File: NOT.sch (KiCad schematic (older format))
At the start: 2 parts, among them U5 4069, U6 4069

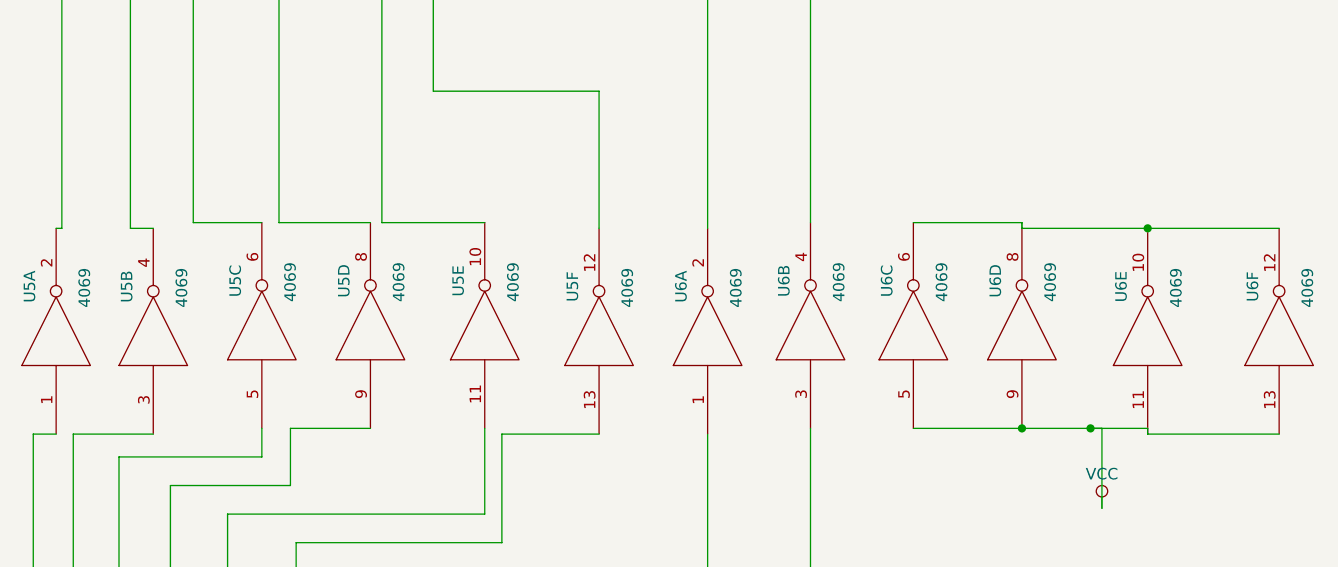
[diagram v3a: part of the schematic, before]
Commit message: fixed duplicate names
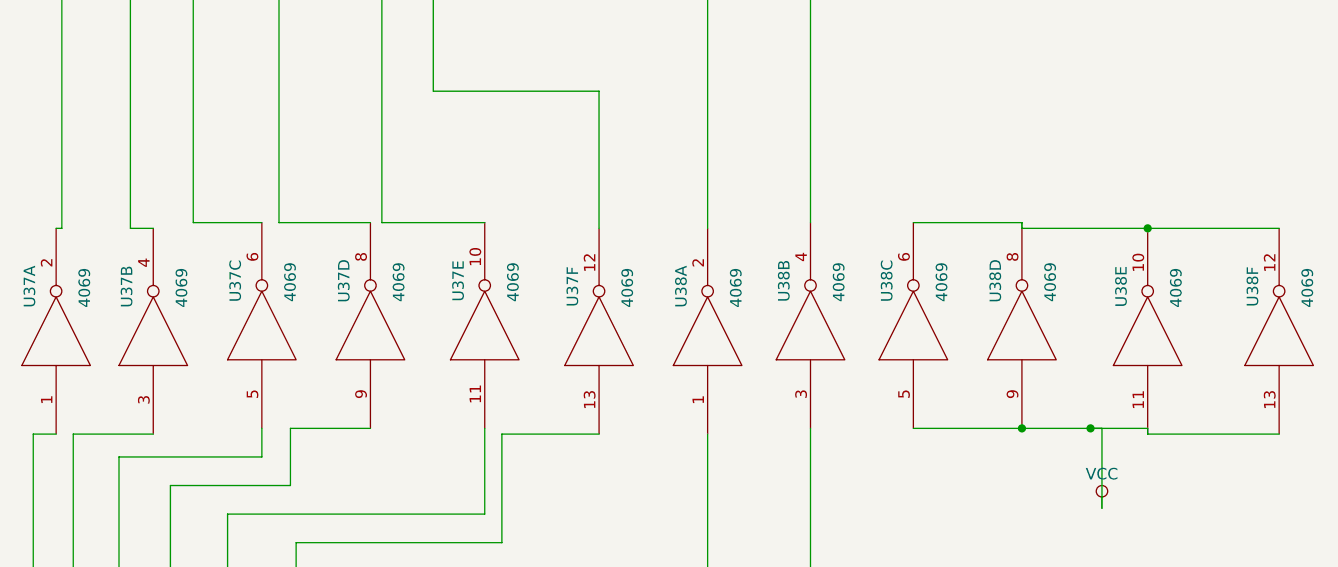
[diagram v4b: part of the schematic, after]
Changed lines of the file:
@@
 $Descr A4 11693 8268
 encoding utf-8
-Sheet 5 21
+Sheet 21 21
 Title ""
 Date ""
@@
 U 1 1 5AE664B9
 P 1025 4250
-F 0 "U5" H 1220 4365 50  0000 C CNN
+AR Path="/5AE62FB7/5AE6649D/5AE664B9" Ref="U5"  Part="1"
+AR Path="/5AE62FB7/5B1BA146/5AE664B9" Ref="U37"  Part="1"
+F 0 "U37" H 1220 4365 50  0000 C CNN
 F 1 "4069" H 1215 4125 50  0000 C CNN
 F 2 "" H 1025 4250 60  0001 C CNN
@@
 U 2 1 5AE6656E
 P 1450 4250
-F 0 "U5" H 1645 4365 50  0000 C CNN
+AR Path="/5AE62FB7/5AE6649D/5AE6656E" Ref="U5"  Part="2"
+AR Path="/5AE62FB7/5B1BA146/5AE6656E" Ref="U37"  Part="2"
+F 0 "U37" H 1645 4365 50  0000 C CNN
 F 1 "4069" H 1640 4125 50  0000 C CNN
 F 2 "" H 1450 4250 60  0001 C CNN
@@
 U 3 1 5AE66605
 P 1925 4225
-F 0 "U5" H 2120 4340 50  0000 C CNN
+AR Path="/5AE62FB7/5AE6649D/5AE66605" Ref="U5"  Part="3"
+AR Path="/5AE62FB7/5B1BA146/5AE66605" Ref="U37"  Part="3"
+F 0 "U37" H 2120 4340 50  0000 C CNN
 F 1 "4069" H 2115 4100 50  0000 C CNN
 F 2 "" H 1925 4225 60  0001 C CNN
@@
 U 4 1 5AE6667C
 P 2400 4225
-F 0 "U5" H 2595 4340 50  0000 C CNN
+AR Path="/5AE62FB7/5AE6649D/5AE6667C" Ref="U5"  Part="4"
+AR Path="/5AE62FB7/5B1BA146/5AE6667C" Ref="U37"  Part="4"
+F 0 "U37" H 2595 4340 50  0000 C CNN
 F 1 "4069" H 2590 4100 50  0000 C CNN
 F 2 "" H 2400 4225 60  0001 C CNN
@@
 U 5 1 5AE66711
 P 2900 4225
-F 0 "U5" H 3095 4340 50  0000 C CNN
+AR Path="/5AE62FB7/5AE6649D/5AE66711" Ref="U5"  Part="5"
+AR Path="/5AE62FB7/5B1BA146/5AE66711" Ref="U37"  Part="5"
+F 0 "U37" H 3095 4340 50  0000 C CNN
 F 1 "4069" H 3090 4100 50  0000 C CNN
 F 2 "" H 2900 4225 60  0001 C CNN
@@
 U 6 1 5AE667CA
 P 3400 4250
-F 0 "U5" H 3595 4365 50  0000 C CNN
+AR Path="/5AE62FB7/5AE6649D/5AE667CA" Ref="U5"  Part="6"
+AR Path="/5AE62FB7/5B1BA146/5AE667CA" Ref="U37"  Part="6"
+F 0 "U37" H 3595 4365 50  0000 C CNN
 F 1 "4069" H 3590 4125 50  0000 C CNN
 F 2 "" H 3400 4250 60  0001 C CNN
@@
 U 1 1 5AE66867
 P 3875 4250
-F 0 "U6" H 4070 4365 50  0000 C CNN
+AR Path="/5AE62FB7/5AE6649D/5AE66867" Ref="U6"  Part="1"
+AR Path="/5AE62FB7/5B1BA146/5AE66867" Ref="U38"  Part="1"
+F 0 "U38" H 4070 4365 50  0000 C CNN
 F 1 "4069" H 4065 4125 50  0000 C CNN
 F 2 "" H 3875 4250 60  0001 C CNN
@@
 U 2 1 5AE668EC
 P 4325 4225
-F 0 "U6" H 4520 4340 50  0000 C CNN
+AR Path="/5AE62FB7/5AE6649D/5AE668EC" Ref="U6"  Part="2"
+AR Path="/5AE62FB7/5B1BA146/5AE668EC" Ref="U38"  Part="2"
+F 0 "U38" H 4520 4340 50  0000 C CNN
 F 1 "4069" H 4515 4100 50  0000 C CNN
 F 2 "" H 4325 4225 60  0001 C CNN
@@
 U 3 1 5AE66989
 P 4775 4225
-F 0 "U6" H 4970 4340 50  0000 C CNN
+AR Path="/5AE62FB7/5AE6649D/5AE66989" Ref="U6"  Part="3"
+AR Path="/5AE62FB7/5B1BA146/5AE66989" Ref="U38"  Part="3"
+F 0 "U38" H 4970 4340 50  0000 C CNN
 F 1 "4069" H 4965 4100 50  0000 C CNN
 F 2 "" H 4775 4225 60  0001 C CNN
@@
 U 4 1 5AE66A24
 P 5250 4225
-F 0 "U6" H 5445 4340 50  0000 C CNN
+AR Path="/5AE62FB7/5AE6649D/5AE66A24" Ref="U6"  Part="4"
+AR Path="/5AE62FB7/5B1BA146/5AE66A24" Ref="U38"  Part="4"
+F 0 "U38" H 5445 4340 50  0000 C CNN
 F 1 "4069" H 5440 4100 50  0000 C CNN
 F 2 "" H 5250 4225 60  0001 C CNN
@@
 U 5 1 5AE66A93
 P 5800 4250
-F 0 "U6" H 5995 4365 50  0000 C CNN
+AR Path="/5AE62FB7/5AE6649D/5AE66A93" Ref="U6"  Part="5"
+AR Path="/5AE62FB7/5B1BA146/5AE66A93" Ref="U38"  Part="5"
+F 0 "U38" H 5995 4365 50  0000 C CNN
 F 1 "4069" H 5990 4125 50  0000 C CNN
 F 2 "" H 5800 4250 60  0001 C CNN
@@
 U 6 1 5AE66B26
 P 6375 4250
-F 0 "U6" H 6570 4365 50  0000 C CNN
+AR Path="/5AE62FB7/5AE6649D/5AE66B26" Ref="U6"  Part="6"
+AR Path="/5AE62FB7/5B1BA146/5AE66B26" Ref="U38"  Part="6"
+F 0 "U38" H 6570 4365 50  0000 C CNN
 F 1 "4069" H 6565 4125 50  0000 C CNN
 F 2 "" H 6375 4250 60  0001 C CNN
@@
 	5800 4700 6375 4700
 $Comp
-L VCC #PWR5
+L VCC #PWR05
 U 1 1 5AE66D66
 P 5600 5025
-F 0 "#PWR5" H 5600 4875 50  0001 C CNN
+AR Path="/5AE62FB7/5AE6649D/5AE66D66" Ref="#PWR05"  Part="1"
+AR Path="/5AE62FB7/5B1BA146/5AE66D66" Ref="#PWR037"  Part="1"
+F 0 "#PWR037" H 5600 4875 50  0001 C CNN
 F 1 "VCC" H 5600 5175 50  0000 C CNN
 F 2 "" H 5600 5025 50  0000 C CNN

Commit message: NC-symbols
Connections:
- now unconnected: U6.10, U6.12, U6.6, U6.8
- no-connect marks 0 -> 4
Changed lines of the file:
@@
 	4325 1625 4325 3775
 Wire Wire Line
-	4775 3775 5250 3775
-Wire Wire Line
-	5250 3800 6375 3800
-Wire Wire Line
 	5250 3775 5250 3800
-Connection ~ 5800 3800
+NoConn ~ 4775 3775
+NoConn ~ 5250 3800
+NoConn ~ 5800 3800
+NoConn ~ 6375 3800
 $EndSCHEMATC

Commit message: spice libs from the internet, opened with new kicad 5.0.0, added spice models to components
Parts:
- U5, U6: symbol 4069 -> myCpu-rescue:4069
- U6: symbol 4069 -> myCpu-rescue:4069; Spice_Lib_File (none) -> cd4000.lib; Spice_Model (none) -> CD4069UB; Spice_Netlist_Enabled (none) -> Y; Spice_Primitive (none) -> X
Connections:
- net VCC: no longer U6.11, U6.13, U6.5, U6.9
- new net: U6.11, U6.13, U6.5, U6.9
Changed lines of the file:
@@
-EESchema Schematic File Version 2
-LIBS:spice
-LIBS:pspice
+EESchema Schematic File Version 4
 LIBS:myCpu-cache
-EELAYER 25 0
+EELAYER 26 0
 EELAYER END
 $Descr A4 11693 8268
 encoding utf-8
-Sheet 21 21
+Sheet 5 21
 Title ""
 Date ""
@@
 Z7
 $Comp
-L 4069 U5
+L myCpu-rescue:4069 U5
 U 1 1 5AE664B9
 P 1025 4250
 AR Path="/5AE62FB7/5AE6649D/5AE664B9" Ref="U5"  Part="1"
 AR Path="/5AE62FB7/5B1BA146/5AE664B9" Ref="U37"  Part="1"
-F 0 "U37" H 1220 4365 50  0000 C CNN
+AR Path="/5AE664B9" Ref="U37"  Part="1"
+F 0 "U5" H 1220 4365 50  0000 C CNN
 F 1 "4069" H 1215 4125 50  0000 C CNN
 F 2 "" H 1025 4250 60  0001 C CNN
@@
 $EndComp
 $Comp
-L 4069 U5
+L myCpu-rescue:4069 U5
 U 2 1 5AE6656E
 P 1450 4250
 AR Path="/5AE62FB7/5AE6649D/5AE6656E" Ref="U5"  Part="2"
 AR Path="/5AE62FB7/5B1BA146/5AE6656E" Ref="U37"  Part="2"
-F 0 "U37" H 1645 4365 50  0000 C CNN
+AR Path="/5AE6656E" Ref="U37"  Part="2"
+F 0 "U5" H 1645 4365 50  0000 C CNN
 F 1 "4069" H 1640 4125 50  0000 C CNN
 F 2 "" H 1450 4250 60  0001 C CNN
@@
 $EndComp
 $Comp
-L 4069 U5
+L myCpu-rescue:4069 U5
 U 3 1 5AE66605
 P 1925 4225
 AR Path="/5AE62FB7/5AE6649D/5AE66605" Ref="U5"  Part="3"
 AR Path="/5AE62FB7/5B1BA146/5AE66605" Ref="U37"  Part="3"
-F 0 "U37" H 2120 4340 50  0000 C CNN
+AR Path="/5AE66605" Ref="U37"  Part="3"
+F 0 "U5" H 2120 4340 50  0000 C CNN
 F 1 "4069" H 2115 4100 50  0000 C CNN
 F 2 "" H 1925 4225 60  0001 C CNN
@@
 $EndComp
 $Comp
-L 4069 U5
+L myCpu-rescue:4069 U5
 U 4 1 5AE6667C
 P 2400 4225
 AR Path="/5AE62FB7/5AE6649D/5AE6667C" Ref="U5"  Part="4"
 AR Path="/5AE62FB7/5B1BA146/5AE6667C" Ref="U37"  Part="4"
-F 0 "U37" H 2595 4340 50  0000 C CNN
+AR Path="/5AE6667C" Ref="U37"  Part="4"
+F 0 "U5" H 2595 4340 50  0000 C CNN
 F 1 "4069" H 2590 4100 50  0000 C CNN
 F 2 "" H 2400 4225 60  0001 C CNN
@@
 $EndComp
 $Comp
-L 4069 U5
+L myCpu-rescue:4069 U5
 U 5 1 5AE66711
 P 2900 4225
 AR Path="/5AE62FB7/5AE6649D/5AE66711" Ref="U5"  Part="5"
 AR Path="/5AE62FB7/5B1BA146/5AE66711" Ref="U37"  Part="5"
-F 0 "U37" H 3095 4340 50  0000 C CNN
+AR Path="/5AE66711" Ref="U37"  Part="5"
+F 0 "U5" H 3095 4340 50  0000 C CNN
 F 1 "4069" H 3090 4100 50  0000 C CNN
 F 2 "" H 2900 4225 60  0001 C CNN
@@
 $EndComp
 $Comp
-L 4069 U5
+L myCpu-rescue:4069 U5
 U 6 1 5AE667CA
 P 3400 4250
 AR Path="/5AE62FB7/5AE6649D/5AE667CA" Ref="U5"  Part="6"
 AR Path="/5AE62FB7/5B1BA146/5AE667CA" Ref="U37"  Part="6"
-F 0 "U37" H 3595 4365 50  0000 C CNN
+AR Path="/5AE667CA" Ref="U37"  Part="6"
+F 0 "U5" H 3595 4365 50  0000 C CNN
 F 1 "4069" H 3590 4125 50  0000 C CNN
 F 2 "" H 3400 4250 60  0001 C CNN
@@
 $EndComp
 $Comp
-L 4069 U6
+L myCpu-rescue:4069 U6
 U 1 1 5AE66867
 P 3875 4250
 AR Path="/5AE62FB7/5AE6649D/5AE66867" Ref="U6"  Part="1"
 AR Path="/5AE62FB7/5B1BA146/5AE66867" Ref="U38"  Part="1"
-F 0 "U38" H 4070 4365 50  0000 C CNN
+AR Path="/5AE66867" Ref="U38"  Part="1"
+F 0 "U6" H 4070 4365 50  0000 C CNN
 F 1 "4069" H 4065 4125 50  0000 C CNN
 F 2 "" H 3875 4250 60  0001 C CNN
@@
 $EndComp
 $Comp
-L 4069 U6
+L myCpu-rescue:4069 U6
 U 2 1 5AE668EC
 P 4325 4225
 AR Path="/5AE62FB7/5AE6649D/5AE668EC" Ref="U6"  Part="2"
 AR Path="/5AE62FB7/5B1BA146/5AE668EC" Ref="U38"  Part="2"
-F 0 "U38" H 4520 4340 50  0000 C CNN
+AR Path="/5AE668EC" Ref="U38"  Part="2"
+F 0 "U6" H 4520 4340 50  0000 C CNN
 F 1 "4069" H 4515 4100 50  0000 C CNN
 F 2 "" H 4325 4225 60  0001 C CNN
@@
 $EndComp
 $Comp
-L 4069 U6
+L myCpu-rescue:4069 U6
 U 3 1 5AE66989
 P 4775 4225
 AR Path="/5AE62FB7/5AE6649D/5AE66989" Ref="U6"  Part="3"
 AR Path="/5AE62FB7/5B1BA146/5AE66989" Ref="U38"  Part="3"
-F 0 "U38" H 4970 4340 50  0000 C CNN
+AR Path="/5AE66989" Ref="U38"  Part="3"
+F 0 "U6" H 4970 4340 50  0000 C CNN
 F 1 "4069" H 4965 4100 50  0000 C CNN
 F 2 "" H 4775 4225 60  0001 C CNN
@@
 $EndComp
 $Comp
-L 4069 U6
+L myCpu-rescue:4069 U6
 U 4 1 5AE66A24
 P 5250 4225
 AR Path="/5AE62FB7/5AE6649D/5AE66A24" Ref="U6"  Part="4"
 AR Path="/5AE62FB7/5B1BA146/5AE66A24" Ref="U38"  Part="4"
-F 0 "U38" H 5445 4340 50  0000 C CNN
+AR Path="/5AE66A24" Ref="U38"  Part="4"
+F 0 "U6" H 5445 4340 50  0000 C CNN
 F 1 "4069" H 5440 4100 50  0000 C CNN
 F 2 "" H 5250 4225 60  0001 C CNN
@@
 $EndComp
 $Comp
-L 4069 U6
+L myCpu-rescue:4069 U6
 U 5 1 5AE66A93
 P 5800 4250
 AR Path="/5AE62FB7/5AE6649D/5AE66A93" Ref="U6"  Part="5"
 AR Path="/5AE62FB7/5B1BA146/5AE66A93" Ref="U38"  Part="5"
-F 0 "U38" H 5995 4365 50  0000 C CNN
+AR Path="/5AE66A93" Ref="U38"  Part="5"
+F 0 "U6" H 5995 4365 50  0000 C CNN
 F 1 "4069" H 5990 4125 50  0000 C CNN
 F 2 "" H 5800 4250 60  0001 C CNN
@@
 $EndComp
 $Comp
-L 4069 U6
+L myCpu-rescue:4069 U6
 U 6 1 5AE66B26
 P 6375 4250
 AR Path="/5AE62FB7/5AE6649D/5AE66B26" Ref="U6"  Part="6"
 AR Path="/5AE62FB7/5B1BA146/5AE66B26" Ref="U38"  Part="6"
-F 0 "U38" H 6570 4365 50  0000 C CNN
+AR Path="/5AE66B26" Ref="U38"  Part="6"
+F 0 "U6" H 6570 4365 50  0000 C CNN
 F 1 "4069" H 6565 4125 50  0000 C CNN
 F 2 "" H 6375 4250 60  0001 C CNN
 F 3 "" H 6375 4250 60  0001 C CNN
+F 4 "X" H 6375 4250 50  0001 C CNN "Spice_Primitive"
+F 5 "CD4069UB" H 6375 4250 50  0001 C CNN "Spice_Model"
+F 6 "Y" H 6375 4250 50  0001 C CNN "Spice_Netlist_Enabled"
+F 7 "cd4000.lib" H 6375 4250 50  0001 C CNN "Spice_Lib_File"
 	6    6375 4250
 	0    -1   -1   0
@@
 	2550 5600 2550 6275
 Wire Wire Line
-	4775 4675 5800 4675
+	4775 4675 5250 4675
 Wire Wire Line
 	5800 4675 5800 4700
@@
 	5800 4700 6375 4700
 $Comp
-L VCC #PWR05
+L myCpu-rescue:VCC #PWR05
 U 1 1 5AE66D66
 P 5600 5025
 AR Path="/5AE62FB7/5AE6649D/5AE66D66" Ref="#PWR05"  Part="1"
 AR Path="/5AE62FB7/5B1BA146/5AE66D66" Ref="#PWR037"  Part="1"
-F 0 "#PWR037" H 5600 4875 50  0001 C CNN
+F 0 "#PWR05" H 5600 4875 50  0001 C CNN
 F 1 "VCC" H 5600 5175 50  0000 C CNN
 F 2 "" H 5600 5025 50  0000 C CNN
@@
 Wire Wire Line
 	5600 5025 5600 4675
-Wire Wire Line
-	5600 4675 5550 4675
-Connection ~ 5550 4675
 Connection ~ 5250 4675
 Wire Wire Line
@@
 NoConn ~ 5800 3800
 NoConn ~ 6375 3800
+Wire Wire Line
+	5250 4675 5800 4675
 $EndSCHEMATC

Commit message: lots of work done
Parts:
- renumbered U5 to U6, U6 to U7
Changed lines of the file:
@@
 $Descr A4 11693 8268
 encoding utf-8
-Sheet 5 21
+Sheet 5 81
 Title ""
 Date ""
@@
 Z7
 $Comp
-L myCpu-rescue:4069 U5
+L myCpu-rescue:4069 U6
 U 1 1 5AE664B9
 P 1025 4250
-AR Path="/5AE62FB7/5AE6649D/5AE664B9" Ref="U5"  Part="1"
-AR Path="/5AE62FB7/5B1BA146/5AE664B9" Ref="U37"  Part="1"
-AR Path="/5AE664B9" Ref="U37"  Part="1"
-F 0 "U5" H 1220 4365 50  0000 C CNN
+AR Path="/5AE62FB7/5AE6649D/5AE664B9" Ref="U6"  Part="1"
+AR Path="/5AE62FB7/5B1BA146/5AE664B9" Ref="U36"  Part="1"
+F 0 "U36" H 1220 4365 50  0000 C CNN
 F 1 "4069" H 1215 4125 50  0000 C CNN
 F 2 "" H 1025 4250 60  0001 C CNN
@@
 $EndComp
 $Comp
-L myCpu-rescue:4069 U5
+L myCpu-rescue:4069 U6
 U 2 1 5AE6656E
 P 1450 4250
-AR Path="/5AE62FB7/5AE6649D/5AE6656E" Ref="U5"  Part="2"
-AR Path="/5AE62FB7/5B1BA146/5AE6656E" Ref="U37"  Part="2"
-AR Path="/5AE6656E" Ref="U37"  Part="2"
-F 0 "U5" H 1645 4365 50  0000 C CNN
+AR Path="/5AE62FB7/5AE6649D/5AE6656E" Ref="U6"  Part="2"
+AR Path="/5AE62FB7/5B1BA146/5AE6656E" Ref="U36"  Part="2"
+F 0 "U36" H 1645 4365 50  0000 C CNN
 F 1 "4069" H 1640 4125 50  0000 C CNN
 F 2 "" H 1450 4250 60  0001 C CNN
@@
 $EndComp
 $Comp
-L myCpu-rescue:4069 U5
+L myCpu-rescue:4069 U6
 U 3 1 5AE66605
 P 1925 4225
-AR Path="/5AE62FB7/5AE6649D/5AE66605" Ref="U5"  Part="3"
-AR Path="/5AE62FB7/5B1BA146/5AE66605" Ref="U37"  Part="3"
-AR Path="/5AE66605" Ref="U37"  Part="3"
-F 0 "U5" H 2120 4340 50  0000 C CNN
+AR Path="/5AE62FB7/5AE6649D/5AE66605" Ref="U6"  Part="3"
+AR Path="/5AE62FB7/5B1BA146/5AE66605" Ref="U36"  Part="3"
+F 0 "U36" H 2120 4340 50  0000 C CNN
 F 1 "4069" H 2115 4100 50  0000 C CNN
 F 2 "" H 1925 4225 60  0001 C CNN
@@
 $EndComp
 $Comp
-L myCpu-rescue:4069 U5
+L myCpu-rescue:4069 U6
 U 4 1 5AE6667C
 P 2400 4225
-AR Path="/5AE62FB7/5AE6649D/5AE6667C" Ref="U5"  Part="4"
-AR Path="/5AE62FB7/5B1BA146/5AE6667C" Ref="U37"  Part="4"
-AR Path="/5AE6667C" Ref="U37"  Part="4"
-F 0 "U5" H 2595 4340 50  0000 C CNN
+AR Path="/5AE62FB7/5AE6649D/5AE6667C" Ref="U6"  Part="4"
+AR Path="/5AE62FB7/5B1BA146/5AE6667C" Ref="U36"  Part="4"
+F 0 "U36" H 2595 4340 50  0000 C CNN
 F 1 "4069" H 2590 4100 50  0000 C CNN
 F 2 "" H 2400 4225 60  0001 C CNN
@@
 $EndComp
 $Comp
-L myCpu-rescue:4069 U5
+L myCpu-rescue:4069 U6
 U 5 1 5AE66711
 P 2900 4225
-AR Path="/5AE62FB7/5AE6649D/5AE66711" Ref="U5"  Part="5"
-AR Path="/5AE62FB7/5B1BA146/5AE66711" Ref="U37"  Part="5"
-AR Path="/5AE66711" Ref="U37"  Part="5"
-F 0 "U5" H 3095 4340 50  0000 C CNN
+AR Path="/5AE62FB7/5AE6649D/5AE66711" Ref="U6"  Part="5"
+AR Path="/5AE62FB7/5B1BA146/5AE66711" Ref="U36"  Part="5"
+F 0 "U36" H 3095 4340 50  0000 C CNN
 F 1 "4069" H 3090 4100 50  0000 C CNN
 F 2 "" H 2900 4225 60  0001 C CNN
@@
 $EndComp
 $Comp
-L myCpu-rescue:4069 U5
+L myCpu-rescue:4069 U6
 U 6 1 5AE667CA
 P 3400 4250
-AR Path="/5AE62FB7/5AE6649D/5AE667CA" Ref="U5"  Part="6"
-AR Path="/5AE62FB7/5B1BA146/5AE667CA" Ref="U37"  Part="6"
-AR Path="/5AE667CA" Ref="U37"  Part="6"
-F 0 "U5" H 3595 4365 50  0000 C CNN
+AR Path="/5AE62FB7/5AE6649D/5AE667CA" Ref="U6"  Part="6"
+AR Path="/5AE62FB7/5B1BA146/5AE667CA" Ref="U36"  Part="6"
+F 0 "U36" H 3595 4365 50  0000 C CNN
 F 1 "4069" H 3590 4125 50  0000 C CNN
 F 2 "" H 3400 4250 60  0001 C CNN
@@
 $EndComp
 $Comp
-L myCpu-rescue:4069 U6
+L myCpu-rescue:4069 U7
 U 1 1 5AE66867
 P 3875 4250
-AR Path="/5AE62FB7/5AE6649D/5AE66867" Ref="U6"  Part="1"
-AR Path="/5AE62FB7/5B1BA146/5AE66867" Ref="U38"  Part="1"
-AR Path="/5AE66867" Ref="U38"  Part="1"
-F 0 "U6" H 4070 4365 50  0000 C CNN
+AR Path="/5AE62FB7/5AE6649D/5AE66867" Ref="U7"  Part="1"
+AR Path="/5AE62FB7/5B1BA146/5AE66867" Ref="U37"  Part="1"
+F 0 "U37" H 4070 4365 50  0000 C CNN
 F 1 "4069" H 4065 4125 50  0000 C CNN
 F 2 "" H 3875 4250 60  0001 C CNN
@@
 $EndComp
 $Comp
-L myCpu-rescue:4069 U6
+L myCpu-rescue:4069 U7
 U 2 1 5AE668EC
 P 4325 4225
-AR Path="/5AE62FB7/5AE6649D/5AE668EC" Ref="U6"  Part="2"
-AR Path="/5AE62FB7/5B1BA146/5AE668EC" Ref="U38"  Part="2"
-AR Path="/5AE668EC" Ref="U38"  Part="2"
-F 0 "U6" H 4520 4340 50  0000 C CNN
+AR Path="/5AE62FB7/5AE6649D/5AE668EC" Ref="U7"  Part="2"
+AR Path="/5AE62FB7/5B1BA146/5AE668EC" Ref="U37"  Part="2"
+F 0 "U37" H 4520 4340 50  0000 C CNN
 F 1 "4069" H 4515 4100 50  0000 C CNN
 F 2 "" H 4325 4225 60  0001 C CNN
@@
 $EndComp
 $Comp
-L myCpu-rescue:4069 U6
+L myCpu-rescue:4069 U7
 U 3 1 5AE66989
 P 4775 4225
-AR Path="/5AE62FB7/5AE6649D/5AE66989" Ref="U6"  Part="3"
-AR Path="/5AE62FB7/5B1BA146/5AE66989" Ref="U38"  Part="3"
-AR Path="/5AE66989" Ref="U38"  Part="3"
-F 0 "U6" H 4970 4340 50  0000 C CNN
+AR Path="/5AE62FB7/5AE6649D/5AE66989" Ref="U7"  Part="3"
+AR Path="/5AE62FB7/5B1BA146/5AE66989" Ref="U37"  Part="3"
+F 0 "U37" H 4970 4340 50  0000 C CNN
 F 1 "4069" H 4965 4100 50  0000 C CNN
 F 2 "" H 4775 4225 60  0001 C CNN
@@
 $EndComp
 $Comp
-L myCpu-rescue:4069 U6
+L myCpu-rescue:4069 U7
 U 4 1 5AE66A24
 P 5250 4225
-AR Path="/5AE62FB7/5AE6649D/5AE66A24" Ref="U6"  Part="4"
-AR Path="/5AE62FB7/5B1BA146/5AE66A24" Ref="U38"  Part="4"
-AR Path="/5AE66A24" Ref="U38"  Part="4"
-F 0 "U6" H 5445 4340 50  0000 C CNN
+AR Path="/5AE62FB7/5AE6649D/5AE66A24" Ref="U7"  Part="4"
+AR Path="/5AE62FB7/5B1BA146/5AE66A24" Ref="U37"  Part="4"
+F 0 "U37" H 5445 4340 50  0000 C CNN
 F 1 "4069" H 5440 4100 50  0000 C CNN
 F 2 "" H 5250 4225 60  0001 C CNN
@@
 $EndComp
 $Comp
-L myCpu-rescue:4069 U6
+L myCpu-rescue:4069 U7
 U 5 1 5AE66A93
 P 5800 4250
-AR Path="/5AE62FB7/5AE6649D/5AE66A93" Ref="U6"  Part="5"
-AR Path="/5AE62FB7/5B1BA146/5AE66A93" Ref="U38"  Part="5"
-AR Path="/5AE66A93" Ref="U38"  Part="5"
-F 0 "U6" H 5995 4365 50  0000 C CNN
+AR Path="/5AE62FB7/5AE6649D/5AE66A93" Ref="U7"  Part="5"
+AR Path="/5AE62FB7/5B1BA146/5AE66A93" Ref="U37"  Part="5"
+F 0 "U37" H 5995 4365 50  0000 C CNN
 F 1 "4069" H 5990 4125 50  0000 C CNN
 F 2 "" H 5800 4250 60  0001 C CNN
@@
 $EndComp
 $Comp
-L myCpu-rescue:4069 U6
+L myCpu-rescue:4069 U7
 U 6 1 5AE66B26
 P 6375 4250
-AR Path="/5AE62FB7/5AE6649D/5AE66B26" Ref="U6"  Part="6"
-AR Path="/5AE62FB7/5B1BA146/5AE66B26" Ref="U38"  Part="6"
-AR Path="/5AE66B26" Ref="U38"  Part="6"
-F 0 "U6" H 6570 4365 50  0000 C CNN
+AR Path="/5AE62FB7/5AE6649D/5AE66B26" Ref="U7"  Part="6"
+AR Path="/5AE62FB7/5B1BA146/5AE66B26" Ref="U37"  Part="6"
+F 0 "U37" H 6570 4365 50  0000 C CNN
 F 1 "4069" H 6565 4125 50  0000 C CNN
 F 2 "" H 6375 4250 60  0001 C CNN
@@
 	5800 4700 6375 4700
 $Comp
-L myCpu-rescue:VCC #PWR05
+L myCpu-rescue:VCC #PWR09
 U 1 1 5AE66D66
 P 5600 5025
-AR Path="/5AE62FB7/5AE6649D/5AE66D66" Ref="#PWR05"  Part="1"
-AR Path="/5AE62FB7/5B1BA146/5AE66D66" Ref="#PWR037"  Part="1"
-F 0 "#PWR05" H 5600 4875 50  0001 C CNN
+AR Path="/5AE62FB7/5AE6649D/5AE66D66" Ref="#PWR09"  Part="1"
+AR Path="/5AE62FB7/5B1BA146/5AE66D66" Ref="#PWR039"  Part="1"
+F 0 "#PWR039" H 5600 4875 50  0001 C CNN
 F 1 "VCC" H 5600 5175 50  0000 C CNN
 F 2 "" H 5600 5025 50  0000 C CNN
